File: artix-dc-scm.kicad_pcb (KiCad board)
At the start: 8 copper layers, 90 x 120.4 mm, 428 parts, among them IC1 TPS54561, J12 S2B-PH-K-S_LF__SN_, J13 62000311121, J2 1-2199230-6, J3 543630489, J4 M20-7830642, J5 SFF-TA-1002-4C+, J6 0878311420, J7 61300611121, Q1 IRLML6402TRPBF, Q10 2N7002, Q11 2N7002, Q12 2N7002, Q13 2N7002, Q14 2N7002, Q15 2N7002, Q16 2N7002, Q2 IRLML6402TRPBF, Q3 IRLML6402TRPBF, Q4 IRLML6402TRPBF, Q5 IRLML6402TRPBF, Q6 IRLML6402TRPBF, Q7 2N7002, Q8 2N7002, Q9 2N7002, U1 DP83848JSQ_NOPB, U10 TPS62823DLCT, U11 TPS62823DLCT, U12 TPS62823DLCT, U13 TPS62823DLCT, U14 XC7A100T-FGG484, U15 SN74LVC1G08DCKR, U16 SN74LS08DBR, U17 EMMC04G-S100-B08U, U18 MAX3421EEHJ, U19 FT245RQ, U2 W25Q32JVSSIQ_TR, U3 W25Q32JVSSIQ_TR, U4 W25Q32JVSSIQ_TR, U5 W25Q32JVSSIQ_TR, U6 NVT2008DQ,115, U7 AS4C256M16D3, U8 TPS51200DRC, U9 LM3881MME_NOPB, Y1 ABM8G-12.000MHZ-18-D2Y-T, Y2 ABM8G-25.000MHZ-18-D2Y-T

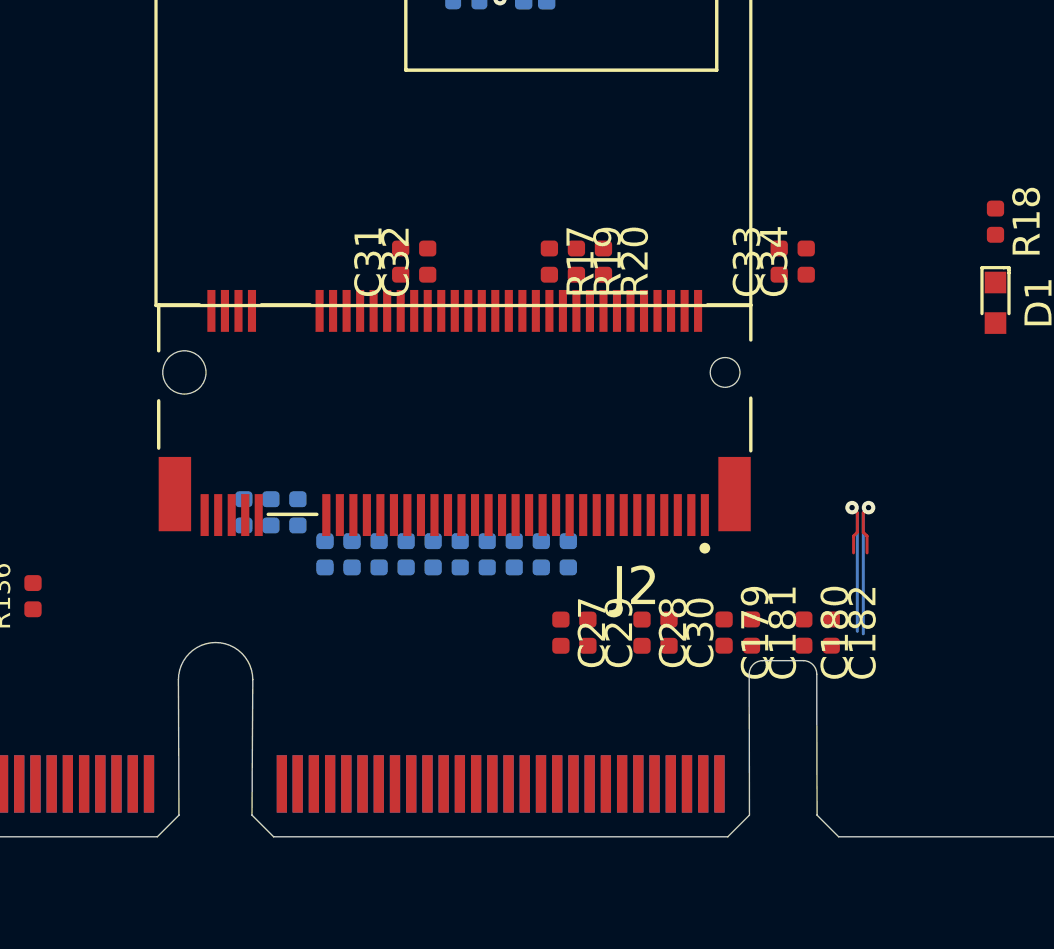
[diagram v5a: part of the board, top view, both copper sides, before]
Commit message: Add net labels to coupled PCIe lanes
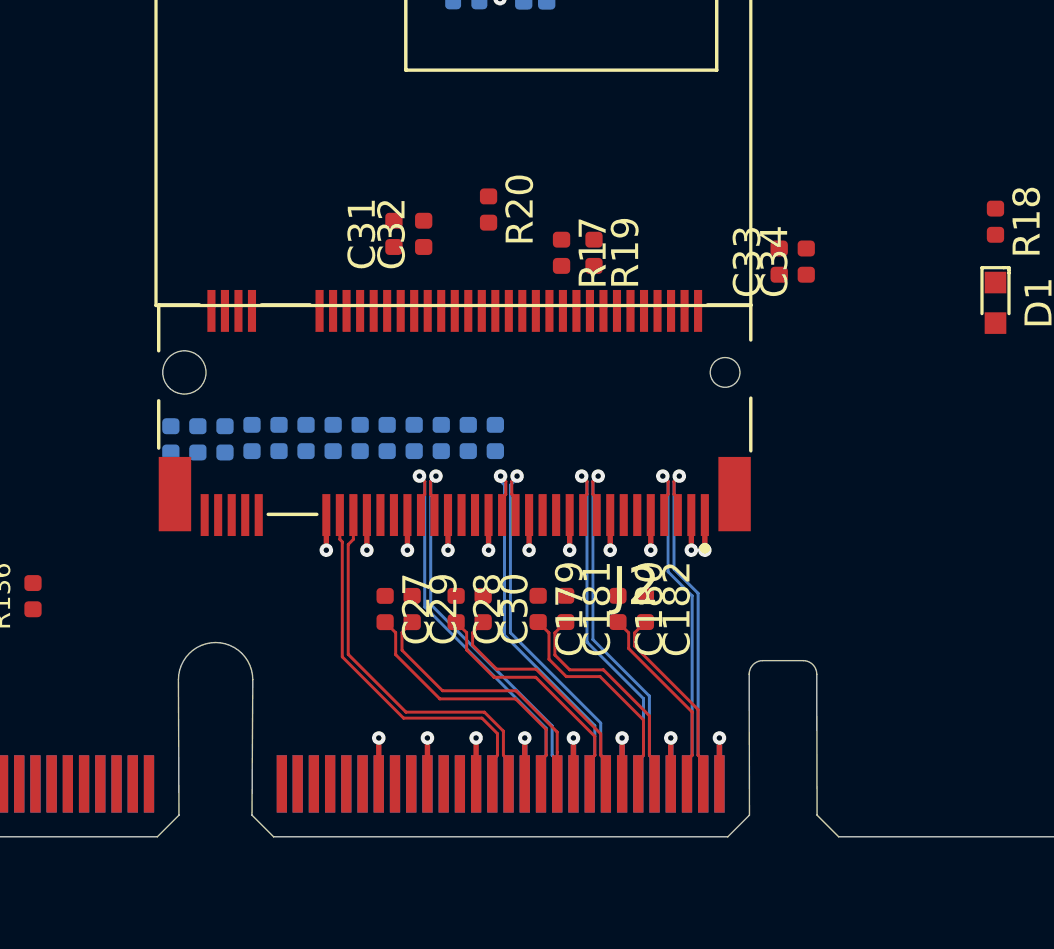
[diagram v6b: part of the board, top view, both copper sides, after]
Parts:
- moved C28 6.93 mm to (126.0, 170.9)
- moved C30 6.93 mm to (127.0, 170.9)
- moved C179 6.93 mm to (129.1, 170.9)
- moved C180 6.93 mm to (132.0, 170.9)
- moved C181 6.93 mm to (130.1, 170.9)
- moved C182 6.93 mm to (133.1, 170.9)
- moved C27 6.56 mm to (123.4, 170.9)
- moved C29 6.56 mm to (124.4, 170.9)
- moved R104 5.08 mm to (118.5, 164.6)
- moved R105 5.08 mm to (119.5, 164.6)
- moved R106 5.08 mm to (120.5, 164.6)
- moved R107 5.08 mm to (121.5, 164.6)
- moved R108 5.08 mm to (122.5, 164.6)
- moved R109 5.08 mm to (123.5, 164.6)
- moved R110 5.08 mm to (124.5, 164.6)
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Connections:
- net Net-(C179-Pad1) renamed /PCIe-connector/PCIE_HPM_TX2_C_P
- net Net-(C180-Pad1) renamed /PCIe-connector/PCIE_HPM_TX3_C_P
- net Net-(C181-Pad1) renamed /PCIe-connector/PCIE_HPM_TX2_C_N
- net Net-(C182-Pad1) renamed /PCIe-connector/PCIE_HPM_TX3_C_N
- net Net-(C27-Pad1) renamed /PCIe-connector/PCIE_HPM_TX0_C_P
- net Net-(C28-Pad1) renamed /PCIe-connector/PCIE_HPM_TX1_C_P
- net Net-(C29-Pad1) renamed /PCIe-connector/PCIE_HPM_TX0_C_N
- net Net-(C30-Pad1) renamed /PCIe-connector/PCIE_HPM_TX1_C_N
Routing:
- net GND: track 11.0 -> 47.4 mm, vias 1 -> 20
- net PCIE_HPM_CLK_N: track 0.00 -> 15.4 mm
- net PCIE_HPM_CLK_P: track 0.00 -> 15.4 mm
- net PCIE_HPM_RX[0]_P: track 0.00 -> 15.0 mm, vias 0 -> 1
- net PCIE_HPM_RX[0]_N: track 0.00 -> 15.0 mm, vias 0 -> 1
- net PCIE_HPM_RX[1]_P: track 0.00 -> 14.6 mm, vias 0 -> 1
- net PCIE_HPM_RX[1]_N: track 0.00 -> 14.5 mm, vias 0 -> 1
- net PCIE_HPM_RX[2]_P: track 0.00 -> 14.0 mm, vias 0 -> 1
- net PCIE_HPM_RX[2]_N: track 0.00 -> 14.0 mm, vias 0 -> 1
- net PCIE_HPM_TX[0]_P: track 0.00 -> 10.2 mm
- net PCIE_HPM_TX[0]_N: track 0.00 -> 10.1 mm
- net PCIE_HPM_TX[2]_P: track 0.00 -> 9.40 mm
- net PCIE_HPM_TX[2]_N: track 0.00 -> 9.37 mm
- net PCIE_HPM_TX[1]_P: track 0.00 -> 9.09 mm
- net PCIE_HPM_TX[1]_N: track 0.00 -> 9.04 mm
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
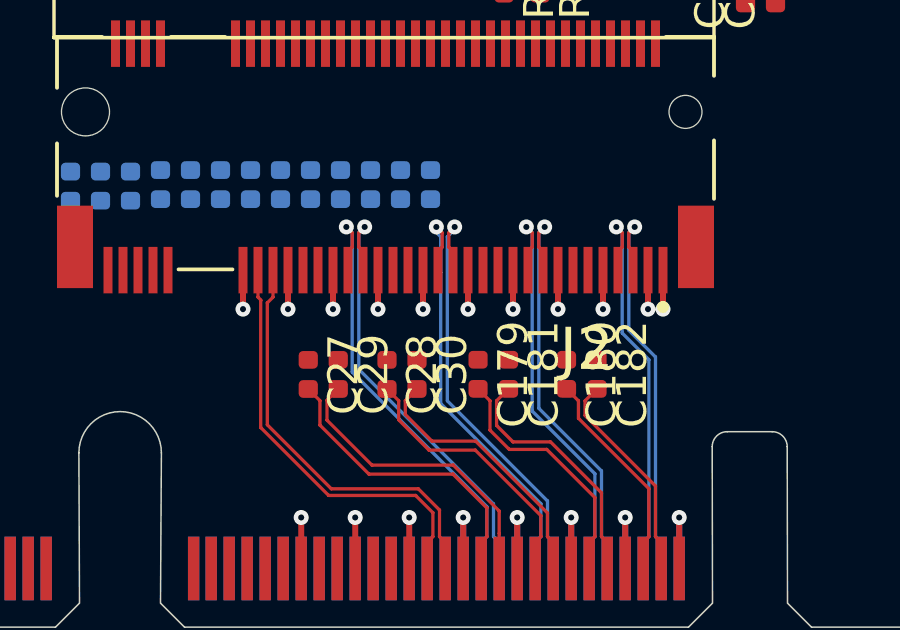
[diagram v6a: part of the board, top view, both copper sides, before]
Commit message: Add layout to M.2 PCIe
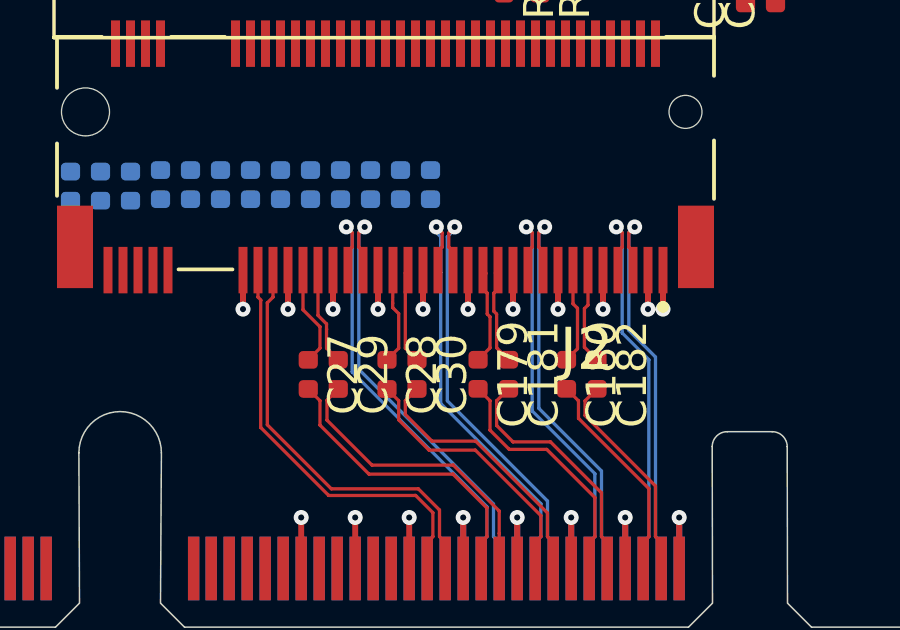
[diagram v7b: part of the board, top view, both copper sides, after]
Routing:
- net /PCIe-connector/PCIE_HPM_TX0_C_P: track 0.00 -> 4.01 mm
- net /PCIe-connector/PCIE_HPM_TX1_C_N: track 0.00 -> 3.96 mm
- net /PCIe-connector/PCIE_HPM_TX0_C_N: track 0.00 -> 3.90 mm
- net /PCIe-connector/PCIE_HPM_TX2_C_P: track 0.00 -> 3.40 mm
- net /PCIe-connector/PCIE_HPM_TX2_C_N: track 0.00 -> 3.38 mm
- net /PCIe-connector/PCIE_HPM_TX1_C_P: track 0.00 -> 3.24 mm
- net /PCIe-connector/PCIE_HPM_TX3_C_N: track 0.00 -> 3.21 mm
- net /PCIe-connector/PCIE_HPM_TX3_C_P: track 0.00 -> 3.20 mm
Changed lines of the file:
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@@
     (thickness 1.6)
     (drawings 64)
-    (tracks 2175)
+    (tracks 2219)
     (zones 0)
     (modules 428)
@@
   )
   (setup
-    (last_trace_width 0.2)
+    (last_trace_width 0.1)
     (user_trace_width 0.15)
     (user_trace_width 0.2)
@@
     (add_net /Interfaces/XI)
     (add_net /Interfaces/XO)
-    (add_net /PCIe-connector/PCIE_HPM_TX0_C_N)
-    (add_net /PCIe-connector/PCIE_HPM_TX0_C_P)
-    (add_net /PCIe-connector/PCIE_HPM_TX1_C_N)
-    (add_net /PCIe-connector/PCIE_HPM_TX1_C_P)
-    (add_net /PCIe-connector/PCIE_HPM_TX2_C_N)
-    (add_net /PCIe-connector/PCIE_HPM_TX2_C_P)
-    (add_net /PCIe-connector/PCIE_HPM_TX3_C_N)
-    (add_net /PCIe-connector/PCIE_HPM_TX3_C_P)
     (add_net "/Power supply/1V0_PG")
     (add_net "/Power supply/1V35_PG")
@@
     (diff_pair_width 0.11)
     (diff_pair_gap 0.11)
+    (add_net /PCIe-connector/PCIE_HPM_TX0_C_N)
+    (add_net /PCIe-connector/PCIE_HPM_TX0_C_P)
+    (add_net /PCIe-connector/PCIE_HPM_TX1_C_N)
+    (add_net /PCIe-connector/PCIE_HPM_TX1_C_P)
+    (add_net /PCIe-connector/PCIE_HPM_TX2_C_N)
+    (add_net /PCIe-connector/PCIE_HPM_TX2_C_P)
+    (add_net /PCIe-connector/PCIE_HPM_TX3_C_N)
+    (add_net /PCIe-connector/PCIE_HPM_TX3_C_P)
     (add_net CLK_100M_PCIE_DN)
     (add_net CLK_100M_PCIE_DP)
@@
     (add_net PCIE_HPM_TX[3]_P)
   )
+  (module artix-dc-scm-footprints:0402-cap (layer F.Cu)
+    (at 123.425 170.876 270)
+    (descr "Resistor SMD 0402 (1005 Metric), square (rectangular) end terminal, IPC_7351 nominal, (Body size source: http://www.tortai-tech.com/upload/download/2011102023233369053.pdf), generated with kicad-footprint-generator")
+    (tags resistor)
+    (attr smd)
+    (fp_text reference C27 (at 0 -1.17 90) (layer F.SilkS)
+      (effects (font (size 1 1) (thickness 0.15)))
+    )
+    (fp_text value C_100n_0402 (at 0 1.17 90) (layer F.Fab)
+      (effects (font (size 1 1) (thickness 0.15)))
+    )
+    (fp_line (start -0.5 0.25) (end -0.5 -0.25) (layer F.Fab) (width 0.1))
+    (fp_line (start -0.5 -0.25) (end 0.5 -0.25) (layer F.Fab) (width 0.1))
+    (fp_line (start 0.5 -0.25) (end 0.5 0.25) (layer F.Fab) (width 0.1))
+    (fp_line (start 0.5 0.25) (end -0.5 0.25) (layer F.Fab) (width 0.1))
+    (fp_line (start -0.93 0.47) (end -0.93 -0.47) (layer F.CrtYd) (width 0.05))
+    (fp_line (start -0.93 -0.47) (end 0.93 -0.47) (layer F.CrtYd) (width 0.05))
+    (fp_line (start 0.93 -0.47) (end 0.93 0.47) (layer F.CrtYd) (width 0.05))
+    (fp_line (start 0.93 0.47) (end -0.93 0.47) (layer F.CrtYd) (width 0.05))
+    (fp_text user %R (at 0 0 90) (layer F.Fab)
+      (effects (font (size 0.25 0.25) (thickness 0.04)))
+    )
+    (pad 2 smd roundrect (at 0.485 0 270) (size 0.59 0.64) (layers F.Cu F.Paste F.Mask) (roundrect_rratio 0.25)
+      (net 558 PCIE_HPM_TX[0]_P))
+    (pad 1 smd roundrect (at -0.485 0 270) (size 0.59 0.64) (layers F.Cu F.Paste F.Mask) (roundrect_rratio 0.25)
+      (net 576 /PCIe-connector/PCIE_HPM_TX0_C_P))
+    (model ${KIPRJMOD}/lib/3d-models/0402-cap.step
+      (offset (xyz 0 0 0.2))
+      (scale (xyz 1 1 1))
+      (rotate (xyz 0 0 0))
+    )
+  )
   (module artix-dc-scm-footprints:1-2199230-6 (layer F.Cu)
     (at 126 162.125 180)
@@
     )
   )
-  (module artix-dc-scm-footprints:0402-cap (layer F.Cu)
-    (at 123.425 170.876 270)
-    (descr "Resistor SMD 0402 (1005 Metric), square (rectangular) end terminal, IPC_7351 nominal, (Body size source: http://www.tortai-tech.com/upload/download/2011102023233369053.pdf), generated with kicad-footprint-generator")
-    (tags resistor)
-    (attr smd)
-    (fp_text reference C27 (at 0 -1.17 90) (layer F.SilkS)
-      (effects (font (size 1 1) (thickness 0.15)))
-    )
-    (fp_text value C_100n_0402 (at 0 1.17 90) (layer F.Fab)
-      (effects (font (size 1 1) (thickness 0.15)))
-    )
-    (fp_line (start -0.5 0.25) (end -0.5 -0.25) (layer F.Fab) (width 0.1))
-    (fp_line (start -0.5 -0.25) (end 0.5 -0.25) (layer F.Fab) (width 0.1))
-    (fp_line (start 0.5 -0.25) (end 0.5 0.25) (layer F.Fab) (width 0.1))
-    (fp_line (start 0.5 0.25) (end -0.5 0.25) (layer F.Fab) (width 0.1))
-    (fp_line (start -0.93 0.47) (end -0.93 -0.47) (layer F.CrtYd) (width 0.05))
-    (fp_line (start -0.93 -0.47) (end 0.93 -0.47) (layer F.CrtYd) (width 0.05))
-    (fp_line (start 0.93 -0.47) (end 0.93 0.47) (layer F.CrtYd) (width 0.05))
-    (fp_line (start 0.93 0.47) (end -0.93 0.47) (layer F.CrtYd) (width 0.05))
-    (fp_text user %R (at 0 0 90) (layer F.Fab)
-      (effects (font (size 0.25 0.25) (thickness 0.04)))
-    )
-    (pad 2 smd roundrect (at 0.485 0 270) (size 0.59 0.64) (layers F.Cu F.Paste F.Mask) (roundrect_rratio 0.25)
-      (net 558 PCIE_HPM_TX[0]_P))
-    (pad 1 smd roundrect (at -0.485 0 270) (size 0.59 0.64) (layers F.Cu F.Paste F.Mask) (roundrect_rratio 0.25)
-      (net 576 /PCIe-connector/PCIE_HPM_TX0_C_P))
-    (model ${KIPRJMOD}/lib/3d-models/0402-cap.step
-      (offset (xyz 0 0 0.2))
-      (scale (xyz 1 1 1))
-      (rotate (xyz 0 0 0))
-    )
-  )
   (module artix-dc-scm-footprints:0402-cap (layer B.Cu)
     (at 70.725 118.375 270)
@@
   (segment (start 135 170.294436) (end 134.11 169.404436) (width 0.11) (layer B.Cu) (net 575))
   (segment (start 134.11 169.404436) (end 134.11 166.154998) (width 0.11) (layer B.Cu) (net 575))
+  (segment (start 123.425 170.391) (end 123.815 170.001) (width 0.11) (layer F.Cu) (net 576))
+  (segment (start 123.25 167.4) (end 123.25 168.025) (width 0.11) (layer F.Cu) (net 576))
+  (segment (start 123.815 170.001) (end 123.815 169.285) (width 0.11) (layer F.Cu) (net 576))
+  (segment (start 123.25 168.72) (end 123.25 167.4) (width 0.11) (layer F.Cu) (net 576))
+  (segment (start 123.815 169.285) (end 123.25 168.72) (width 0.11) (layer F.Cu) (net 576))
+  (segment (start 126.24 168.5) (end 126.25 167.4) (width 0.11) (layer F.Cu) (net 577))
+  (segment (start 126.24 168.65) (end 126.24 168.5) (width 0.11) (layer F.Cu) (net 577))
+  (segment (start 126.05 170.391) (end 126.44 170.001) (width 0.11) (layer F.Cu) (net 577))
+  (segment (start 126.44 168.85) (end 126.24 168.65) (width 0.11) (layer F.Cu) (net 577))
+  (segment (start 126.44 170.001) (end 126.44 168.85) (width 0.11) (layer F.Cu) (net 577))
+  (segment (start 124.425 170.391) (end 124.035 170.001) (width 0.11) (layer F.Cu) (net 578))
+  (segment (start 123.75 167.4) (end 123.75 168.025) (width 0.11) (layer F.Cu) (net 578))
+  (segment (start 124.035009 169.376131) (end 124.035009 169.193869) (width 0.11) (layer F.Cu) (net 578))
+  (segment (start 124.035 170.001) (end 124.035 169.37614) (width 0.11) (layer F.Cu) (net 578))
+  (segment (start 124.035 169.37614) (end 124.035009 169.376131) (width 0.11) (layer F.Cu) (net 578))
+  (segment (start 123.75 168.90886) (end 123.75 167.4) (width 0.11) (layer F.Cu) (net 578))
+  (segment (start 124.035009 169.193869) (end 123.75 168.90886) (width 0.11) (layer F.Cu) (net 578))
+  (segment (start 126.75 168.025) (end 126.65 168.125) (width 0.1) (layer F.Cu) (net 579))
+  (segment (start 126.75 167.4) (end 126.75 168.025) (width 0.1) (layer F.Cu) (net 579))
+  (segment (start 126.66 167.49) (end 126.75 167.4) (width 0.11) (layer F.Cu) (net 579))
+  (segment (start 127.05 170.391) (end 126.66 170.001) (width 0.11) (layer F.Cu) (net 579))
+  (segment (start 126.66 170.001) (end 126.66 167.49) (width 0.11) (layer F.Cu) (net 579))
+  (segment (start 129.25 167.4) (end 129.36 167.51) (width 0.11) (layer F.Cu) (net 580))
+  (segment (start 129.39 168.165) (end 129.25 168.025) (width 0.11) (layer F.Cu) (net 580))
+  (segment (start 129.39 168.861141) (end 129.39 168.165) (width 0.11) (layer F.Cu) (net 580))
+  (segment (start 129.484 168.955141) (end 129.39 168.861141) (width 0.11) (layer F.Cu) (net 580))
+  (segment (start 129.25 168.025) (end 129.25 167.4) (width 0.11) (layer F.Cu) (net 580))
+  (segment (start 129.484 169.989) (end 129.484 168.955141) (width 0.11) (layer F.Cu) (net 580))
+  (segment (start 129.086 170.387) (end 129.484 169.989) (width 0.11) (layer F.Cu) (net 580))
+  (segment (start 132.4 168.67) (end 132.25 168.52) (width 0.11) (layer F.Cu) (net 581))
+  (segment (start 132.25 168.52) (end 132.25 167.4) (width 0.11) (layer F.Cu) (net 581))
+  (segment (start 132.034 170.387) (end 132.4 170.021) (width 0.11) (layer F.Cu) (net 581))
+  (segment (start 132.4 170.021) (end 132.4 168.67) (width 0.11) (layer F.Cu) (net 581))
+  (segment (start 129.66 167.49) (end 129.75 167.4) (width 0.11) (layer F.Cu) (net 582))
+  (segment (start 129.75 168.025) (end 129.75 167.4) (width 0.11) (layer F.Cu) (net 582))
+  (segment (start 129.61 168.165) (end 129.75 168.025) (width 0.11) (layer F.Cu) (net 582))
+  (segment (start 129.704 168.864) (end 129.61 168.77) (width 0.11) (layer F.Cu) (net 582))
+  (segment (start 129.704 169.989) (end 129.704 168.864) (width 0.11) (layer F.Cu) (net 582))
+  (segment (start 129.61 168.77) (end 129.61 168.165) (width 0.11) (layer F.Cu) (net 582))
+  (segment (start 130.102 170.387) (end 129.704 169.989) (width 0.11) (layer F.Cu) (net 582))
+  (segment (start 132.75 168.562501) (end 132.75 167.4) (width 0.11) (layer F.Cu) (net 583))
+  (segment (start 132.63 168.682501) (end 132.75 168.562501) (width 0.11) (layer F.Cu) (net 583))
+  (segment (start 133.05 170.387) (end 132.63 169.967) (width 0.11) (layer F.Cu) (net 583))
+  (segment (start 132.63 169.967) (end 132.63 168.682501) (width 0.11) (layer F.Cu) (net 583))
   (zone (net 0) (net_name "") (layers F.Cu GND1 In2.Cu VCC1 GND2 B.Cu) (hatch edge 0.508)
     (connect_pads (clearance 0.508))
